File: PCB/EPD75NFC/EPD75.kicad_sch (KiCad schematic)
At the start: 149 parts, among them J1 Conn_01x26, J10 TF_PUSH, J11 Reset, J12 TC2030-USB-NL-DS, J2 PWR, J3 NFC, J4 BTN, J5 USB-C-Socket-H, J7 USB-C-Socket-H, J8 PWR, Q1 BSS138, SW2 Tamper, U2 PN532, U3 MD8942, U4 ESP32-S3-MINI-1, Y1 27.12MHz

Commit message: Tidy for new inductor
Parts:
- removed JP2: SolderJumper_3_Bridged12, RevK:SolderJumper3, symbol Jumper:SolderJumper_3_Bridged12
- removed R2: 3R, RevK:R_0402, symbol Device:R
- added C67: 220uF Tant, RevK:CP_EIA-3528-21_Kemet-B, symbol Device:C_Polarized
- added C68, C69: 22uF, RevK:C_0603, symbol Device:C
- added C70: 100nF, RevK:C_0402, symbol Device:C
- C17, C18: value 4.7uF -> 4.7uF 50V; footprint RevK:C_0402 -> RevK:C_0805
- L1: value 10uH -> 470uH; MPN (none) -> C42429207
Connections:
- net +3.3V: now also C67.1, C68.2, C69.2, C70.2
- net D-: now also J12.2 (NC), J12.6 (NC)
- net GND: now also C67.2, C68.1, C69.1, C70.1; no longer J12.6 (GND)
- net VBUS: no longer J12.2 (VBUS)
- net at R1.1: now also J1.3 (Pin_3), Q1.2 (S)
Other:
- moved on the sheet: R1

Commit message: Tamper
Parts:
- SW2: value Tamper -> ESE13V01D; footprint RevK:SW_Push_1P1T_NO_6x6mm -> RevK:ESE13; Manufacturer (none) -> Panasonic; Part No (none) -> ESE13V01D; now in the parts list
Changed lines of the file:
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@@
+	)
+	(symbol
+		(lib_id "Switch:SW_Push")
+		(at 481.965 142.875 0)
+		(unit 1)
+		(exclude_from_sim no)
+		(in_bom yes)
+		(on_board yes)
+		(dnp no)
+		(property "Reference" "SW2"
+			(at 481.965 135.636 0)
+			(effects
+				(font
+					(size 1.27 1.27)
+				)
+			)
+		)
+		(property "Value" "ESE13V01D"
+			(at 481.965 137.9474 0)
+			(effects
+				(font
+					(size 1.27 1.27)
+				)
+			)
+		)
+		(property "Footprint" "RevK:ESE13"
+			(at 481.965 137.795 0)
+			(effects
+				(font
+					(size 1.27 1.27)
+				)
+				(hide yes)
+			)
+		)
+		(property "Datasheet" "https://docs.rs-online.com/73f9/0900766b810acfc9.pdf"
+			(at 481.965 137.795 0)
+			(effects
+				(font
+					(size 1.27 1.27)
+				)
+				(hide yes)
+			)
+		)
+		(property "Description" ""
+			(at 481.965 142.875 0)
+			(effects
+				(font
+					(size 1.27 1.27)
+				)
+				(hide yes)
+			)
+		)
+		(property "Part No" "ESE13V01D"
+			(at 481.965 142.875 0)
+			(effects
+				(font
+					(size 1.27 1.27)
+				)
+				(hide yes)
+			)
+		)
+		(property "Manufacturer" "Panasonic"
+			(at 481.965 142.875 0)
+			(effects
+				(font
+					(size 1.27 1.27)
+				)
+				(hide yes)
+			)
+		)
+		(pin "1"
+		)
+		(pin "2"
+		)
+		(instances
+			(project "EPD75"
+				(path "/46c350bb-7de4-4e81-aafd-4af55e37aab0"
+					(reference "SW2")
+					(unit 1)
+				)
+			)
+		)
 	)
 	(symbol
@@
 					(unit 1)
 				)
-			)
-		)
-	)
-	(symbol
-		(lib_id "Switch:SW_Push")
-		(at 481.965 142.875 0)
-		(unit 1)
-		(exclude_from_sim no)
-		(in_bom no)
-		(on_board yes)
-		(dnp no)
-		(fields_autoplaced yes)
-		(property "Reference" "SW2"
-			(at 481.965 135.8095 0)
-			(effects
-				(font
-					(size 1.27 1.27)
-				)
-			)
-		)
-		(property "Value" "Tamper"
-			(at 481.965 138.2338 0)
-			(effects
-				(font
-					(size 1.27 1.27)
-				)
-			)
-		)
-		(property "Footprint" "RevK:SW_Push_1P1T_NO_6x6mm"
-			(at 481.965 137.795 0)
-			(effects
-				(font
-					(size 1.27 1.27)
-				)
-				(hide yes)
-			)
-		)
-		(property "Datasheet" "~"
-			(at 481.965 137.795 0)
-			(effects
-				(font
-					(size 1.27 1.27)
-				)
-				(hide yes)
-			)
-		)
-		(property "Description" "Push button switch, generic, two pins"
-			(at 481.965 142.875 0)
-			(effects
-				(font
-					(size 1.27 1.27)
-				)
-				(hide yes)
-			)
-		)
-		(pin "1"
-		)
-		(pin "2"
-		)
-		(instances
-			(project "EPD75"
-				(path "/46c350bb-7de4-4e81-aafd-4af55e37aab0"
-					(reference "SW2")
-					(unit 1)
-				)

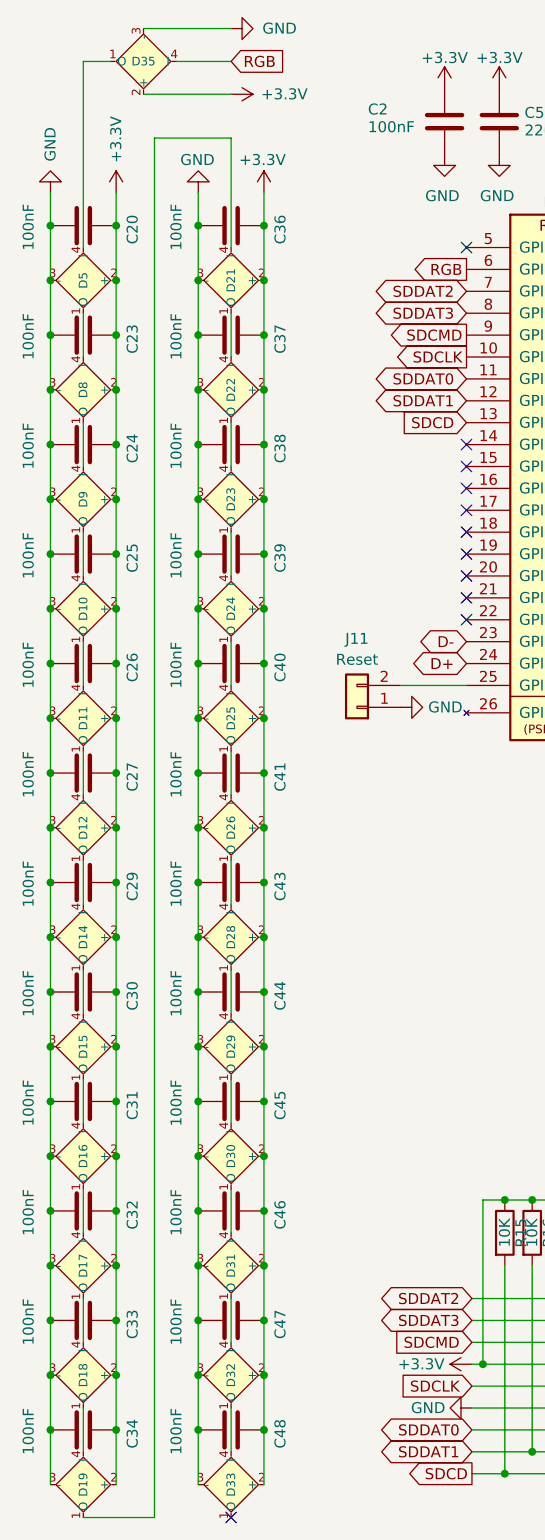
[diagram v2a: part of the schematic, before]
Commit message: New LEDs
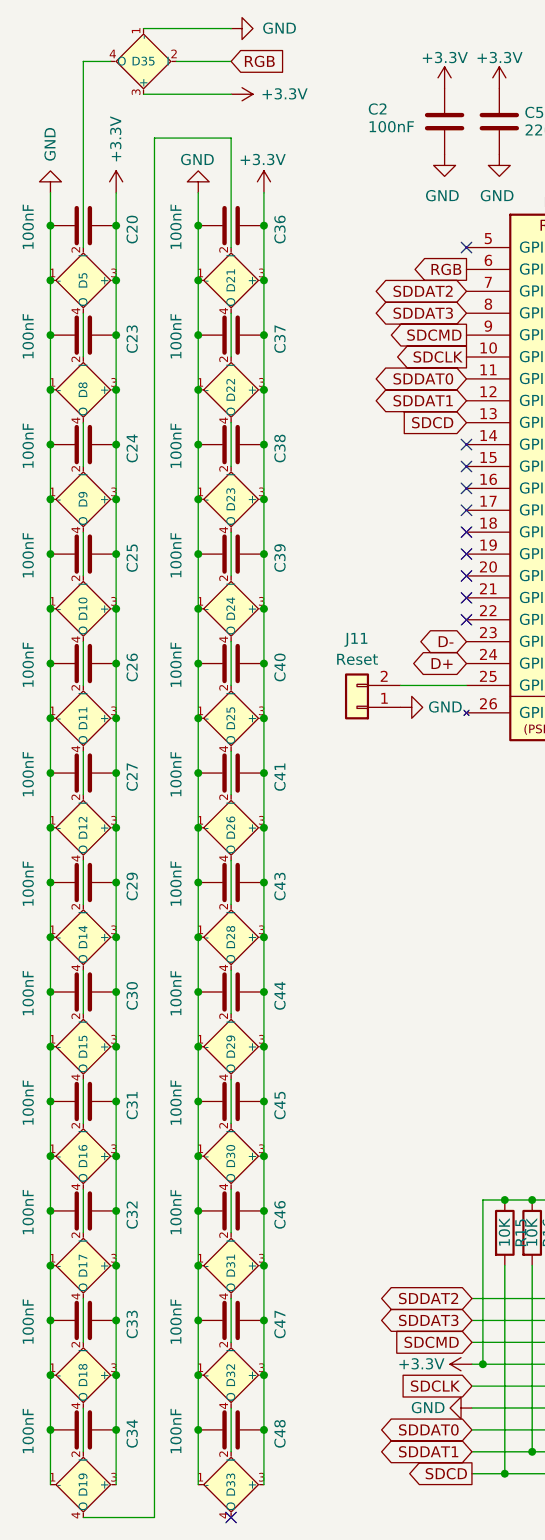
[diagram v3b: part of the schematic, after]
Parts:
- D10, D11, D12, D14, D15, D16, D17, D18, D19, D21, D22, D23, D24, D25, D26, D28, D29, D30, D31, D32, D33, D35, D5, D8, D9: footprint RevK:SMD1010 -> RevK:SMD1615; symbol RevK:WS2812B-1mm -> RevK:WS2812B-1.5mm; MPN C5349953 -> C5349954
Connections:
- net +3.3V: now also D10.3 (+), D11.3 (+), D12.3 (+), D14.3 (+), D15.3 (+), D16.3 (+), D17.3 (+), D18.3 (+), D19.3 (+), D21.3 (+), D22.3 (+), D23.3 (+), D24.3 (+), D25.3 (+), D26.3 (+), D28.3 (+), D29.3 (+), D30.3 (+), D31.3 (+), D32.3 (+), D33.3 (+), D35.3 (+), D5.3 (+), D8.3 (+), D9.3 (+); no longer D10.2 (+), D11.2 (+), D12.2 (+), D14.2 (+), D15.2 (+), D16.2 (+), D17.2 (+), D18.2 (+), D19.2 (+), D21.2 (+), D22.2 (+), D23.2 (+), D24.2 (+), D25.2 (+), D26.2 (+), D28.2 (+), D29.2 (+), D30.2 (+), D31.2 (+), D32.2 (+), D33.2 (+), D35.2 (+), D5.2 (+), D8.2 (+), D9.2 (+)
- net GND: now also D10.1 (-), D11.1 (-), D12.1 (-), D14.1 (-), D15.1 (-), D16.1 (-), D17.1 (-), D18.1 (-), D19.1 (-), D21.1 (-), D22.1 (-), D23.1 (-), D24.1 (-), D25.1 (-), D26.1 (-), D28.1 (-), D29.1 (-), D30.1 (-), D31.1 (-), D32.1 (-), D33.1 (-), D35.1 (-), D5.1 (-), D8.1 (-), D9.1 (-); no longer D10.3 (-), D11.3 (-), D12.3 (-), D14.3 (-), D15.3 (-), D16.3 (-), D17.3 (-), D18.3 (-), D19.3 (-), D21.3 (-), D22.3 (-), D23.3 (-), D24.3 (-), D25.3 (-), D26.3 (-), D28.3 (-), D29.3 (-), D30.3 (-), D31.3 (-), D32.3 (-), D33.3 (-), D35.3 (-), D5.3 (-), D8.3 (-), D9.3 (-)
- net RGB: now also D35.2 (I); no longer D35.4 (I)
- net at D22.4 (O): now also D23.2 (I); no longer D21.1 (O)
- net at D21.4 (O): now also D22.2 (I); no longer D19.1 (O)
- net at D19.4 (O): now also D21.2 (I); no longer D18.1 (O)
- net at D23.4 (O): now also D24.2 (I); no longer D22.1 (O)
- net at D30.4 (O): now also D31.2 (I); no longer D29.1 (O)
- net at D29.4 (O): now also D30.2 (I); no longer D28.1 (O)
- net at D24.4 (O): now also D25.2 (I); no longer D23.1 (O)
- net at D28.4 (O): now also D29.2 (I); no longer D26.1 (O)
- net at D26.4 (O): now also D28.2 (I); no longer D25.1 (O)
- net at D17.4 (O): now also D18.2 (I); no longer D16.1 (O)
- net at D16.4 (O): now also D17.2 (I); no longer D15.1 (O)
- net at D18.4 (O): now also D19.2 (I); no longer D17.1 (O)
- net at D14.4 (O): now also D15.2 (I); no longer D12.1 (O)
- net at D12.4 (O): now also D14.2 (I); no longer D11.1 (O)
- net at D31.4 (O): now also D32.2 (I); no longer D30.1 (O)
- net at D33.4 (O): no longer D32.1 (O)
- net at D32.4 (O): now also D33.2 (I); no longer D31.1 (O)
- net at D9.4 (O): now also D10.2 (I); no longer D8.1 (O)
- net at D8.4 (O): now also D9.2 (I); no longer D5.1 (O)
- net at D25.4 (O): now also D26.2 (I); no longer D24.1 (O)
- net at D11.4 (O): now also D12.2 (I); no longer D10.1 (O)
- net at D5.4 (O): now also D8.2 (I); no longer D35.1 (O)
- net at D15.4 (O): now also D16.2 (I); no longer D14.1 (O)
- net at D10.4 (O): now also D11.2 (I); no longer D9.1 (O)
- new net: D35.4 (O), D5.2 (I)
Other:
- moved on the sheet: D10, D11, D12, D14, D15, D16, D17, D18, D19, D21, D22, D23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

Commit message: Regulator update
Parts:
- removed C10: 100nF, RevK:C_0603_, symbol RevK:Hidden
- removed C8: 10uF 35V, RevK:C_0603_, symbol RevK:Hidden
- removed C9: 10uF 6.3V, RevK:C_0603_, symbol RevK:Hidden
- removed L2: 10uH, RevK:L_4x4_, symbol RevK:Hidden
- removed R10: 39k2, RevK:R_0402_, symbol RevK:Hidden
- removed R11: 1M, RevK:R_0402_, symbol RevK:Hidden
- removed R9: 124k, RevK:R_0402_, symbol RevK:Hidden
- removed U3: MD8942, RevK:SOT-23-6-MD8942, symbol RevK:MD89420-RegBlock
- added C21: 22uF 25V, RevK:C_0805, symbol Device:C
- added C71, C72: 100nF 25V, RevK:C_0402, symbol Device:C
- added C73, C76, C77, C78, C79, C80: 100nF, RevK:C_0201, symbol Device:C
- added C74: 18pF, RevK:C_0201, symbol Device:C
- added C75: 47uF 6V, RevK:C_0805, symbol Device:C
- added L5: 4.7uH, RevK:L_5x5, symbol Device:L
- added R14, R2: 150k 1%, RevK:R_0201, symbol Device:R
- added R29: 33k 1%, RevK:R_0201, symbol Device:R
- added U1: TPS562246, RevK:SOT-563, symbol RevK:TPS562246
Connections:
- net +3.3V: now also C74.2, C75.1, C76.2, C77.2, C78.2, C79.2, C80.2, L5.2, R14.1
- net GND: now also C21.2, C71.2, C72.2, C75.2, C76.1, C77.1, C78.1, C79.1, C80.1, R29.2, U1.3 (GND)
- net PWR: now also C21.1, C71.1, C72.1, R2.2, U1.1 (VIN)
- new net BST: C73.1, U1.4 (VBST)
- new net EN: R2.1, U1.5 (EN)
- new net FB: C74.1, R14.2, R29.1, U1.6 (VFB)
- new net SW: C73.2, L5.1, U1.2 (SW)
- no-connect marks 41 -> 40
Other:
- moved on the sheet: C19, C22, D34, J4, J8, R7

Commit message: Library update
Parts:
- L1: footprint RevK:L_4x4 -> RevK:L_6x6; MPN C42429207 -> C168100
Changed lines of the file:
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@@
 			)
 		)
-		(property "Footprint" "RevK:L_4x4"
+		(property "Footprint" "RevK:L_6x6"
 			(at 187.96 93.98 0)
 			(effects
@@
 			)
 		)
-		(property "MPN" "C42429207"
+		(property "MPN" "C168100"
 			(at 187.96 93.98 0)
 			(effects

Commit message: Library update
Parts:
- added C8, C81, C83, C9: 100nF, RevK:C_0201, symbol Device:C
- added T1: T3902_MEMS_Mic, RevK:T3902_MEMS_Mic_Open, symbol RevK:T3902_MEMS_Mic
- added U3: SCD41, RevK:SCD41, symbol RevK:SCD41
- added U5: GZP6816D, RevK:Bosch_LGA-8_2x2.5mm_P0.65mm_ClockwisePinNumbering, symbol RevK:GZP6816D
- added U7: SHT40, RevK:Sensirion_DFN-4_1.5x1.5mm_P0.5mm_SHT4x-Side, symbol RevK:SHT40
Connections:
- net +3.3V: now also C8.2, C81.2, C83.2, C9.2, T1.2 (SELECT), T1.5 (VDD), U3.19 (VDDH), U3.7 (VDD), U5.8 (VDD), U7.3 (VDD)
- net GND: now also C8.1, C81.1, C83.1, C9.1, T1.3 (GND), U3.20 (GND), U3.21 (GND), U3.6 (GND), U5.1 (GND), U5.7 (GND), U7.4 (VSS)
- net SCL: now reaches U4.19 (GPIO15)
- net SCL: now also U3.9 (SCL), U5.4 (SCL), U7.2 (SCL)
- net SDA: now reaches U4.20 (GPIO16)
- net SDA: now also U3.10 (SDA), U5.3 (SDA), U7.1 (SDA)
- net MDATA: now reaches U4.21 (GPIO17)
- net MDATA: now also T1.1 (DATA)
- net MCLK: now reaches U4.22 (GPIO18)
- net MCLK: now also T1.4 (CLK)
- no-connect marks 40 -> 36
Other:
- note added: "Left"
- moved on the sheet: A1, C35, C42, C49, C50, C51, C52, C53, C54, C55, C56, C57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

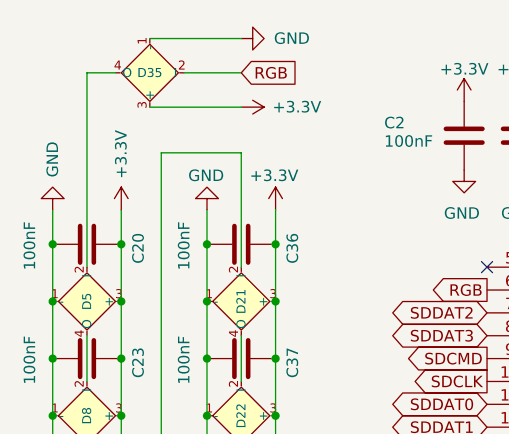
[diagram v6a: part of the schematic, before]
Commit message: Updated NFC, and re-render
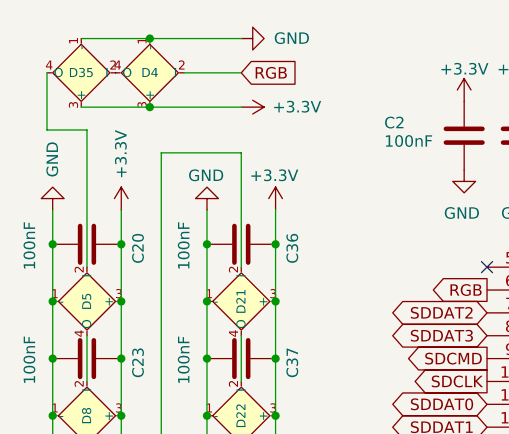
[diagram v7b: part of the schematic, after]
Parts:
- added D4: XL-1010RGBC-WS2812B, RevK:SMD1615, symbol RevK:WS2812B-1.5mm
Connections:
- net +3.3V: now also D4.3 (+)
- net GND: now also D4.1 (-)
- net RGB: now also D4.2 (I); no longer D35.2 (I)
- new net: D35.2 (I), D4.4 (O)
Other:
- moved on the sheet: D35
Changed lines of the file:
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@@
 	)
 	(junction
+		(at 31.115 16.51)
+		(diameter 0)
+		(color 0 0 0 0)
+	)
+	(junction
 		(at 27.94 77.47)
 		(diameter 0)
@@
 	)
 	(junction
+		(at 31.115 24.13)
+		(diameter 0)
+		(color 0 0 0 0)
+	)
+	(junction
 		(at 269.24 37.465)
 		(diameter 0)
@@
 	(wire
 		(pts
+			(xy 23.495 16.51) (xy 31.115 16.51)
+		)
+		(stroke
+			(width 0)
+			(type default)
+		)
+	)
+	(wire
+		(pts
 			(xy 204.47 271.145) (xy 204.47 303.53)
 		)
@@
 	(wire
 		(pts
+			(xy 31.115 16.51) (xy 41.275 16.51)
+		)
+		(stroke
+			(width 0)
+			(type default)
+		)
+	)
+	(wire
+		(pts
 			(xy 41.275 181.61) (xy 41.275 176.53)
 		)
@@
 	(wire
 		(pts
+			(xy 19.685 20.32) (xy 19.685 26.67)
+		)
+		(stroke
+			(width 0)
+			(type default)
+		)
+	)
+	(wire
+		(pts
 			(xy 20.32 71.12) (xy 20.32 77.47)
 		)
@@
 	(wire
 		(pts
-			(xy 27.305 20.32) (xy 24.13 20.32)
-		)
-		(stroke
-			(width 0)
-			(type default)
-		)
-	)
-	(wire
-		(pts
 			(xy 20.32 39.37) (xy 20.32 45.72)
 		)
@@
 	(wire
 		(pts
+			(xy 23.495 24.13) (xy 31.115 24.13)
+		)
+		(stroke
+			(width 0)
+			(type default)
+		)
+	)
+	(wire
+		(pts
 			(xy 37.465 58.42) (xy 37.465 64.77)
 		)
@@
 	(wire
 		(pts
-			(xy 31.115 16.51) (xy 41.275 16.51)
+			(xy 184.785 27.305) (xy 186.055 27.305)
 		)
 		(stroke
@@
 	(wire
 		(pts
-			(xy 184.785 27.305) (xy 186.055 27.305)
+			(xy 27.94 35.56) (xy 27.94 39.37)
 		)
 		(stroke
@@
 	(wire
 		(pts
-			(xy 27.94 35.56) (xy 27.94 39.37)
+			(xy 70.485 171.45) (xy 96.52 171.45)
 		)
 		(stroke
@@
 	(wire
 		(pts
-			(xy 70.485 171.45) (xy 96.52 171.45)
+			(xy 37.465 147.32) (xy 37.465 153.67)
 		)
 		(stroke
@@
 	(wire
 		(pts
-			(xy 37.465 147.32) (xy 37.465 153.67)
+			(xy 37.465 83.82) (xy 37.465 90.17)
 		)
 		(stroke
@@
 	(wire
 		(pts
-			(xy 37.465 83.82) (xy 37.465 90.17)
+			(xy 24.13 26.67) (xy 24.13 41.91)
 		)
 		(stroke
@@
 	(wire
 		(pts
-			(xy 24.13 20.32) (xy 24.13 41.91)
-		)
-		(stroke
-			(width 0)
-			(type default)
-		)
-	)
-	(wire
-		(pts
 			(xy 144.145 207.01) (xy 153.035 207.01)
 		)
@@
 	(wire
 		(pts
+			(xy 31.115 24.13) (xy 41.275 24.13)
+		)
+		(stroke
+			(width 0)
+			(type default)
+		)
+	)
+	(wire
+		(pts
 			(xy 235.585 282.575) (xy 231.775 282.575)
 		)
@@
 	(wire
 		(pts
+			(xy 19.685 26.67) (xy 24.13 26.67)
+		)
+		(stroke
+			(width 0)
+			(type default)
+		)
+	)
+	(wire
+		(pts
 			(xy 99.06 95.885) (xy 105.41 95.885)
 		)
@@
 	(wire
 		(pts
-			(xy 31.115 24.13) (xy 41.275 24.13)
-		)
-		(stroke
-			(width 0)
-			(type default)
-		)
-	)
-	(wire
-		(pts
 			(xy 114.935 268.605) (xy 139.065 268.605)
 		)
@@
 	)
 	(symbol
+		(lib_id "RevK:WS2812B-1.5mm")
+		(at 31.115 20.32 180)
+		(unit 1)
+		(exclude_from_sim no)
+		(in_bom yes)
+		(on_board yes)
+		(dnp no)
+		(property "Reference" "D4"
+			(at 31.115 20.32 0)
+			(do_not_autoplace yes)
+			(effects
+				(font
+					(size 1 1)
+				)
+			)
+		)
+		(property "Value" "XL-1010RGBC-WS2812B"
+			(at 29.845 14.605 0)
+			(effects
+				(font
+					(size 1 1)
+				)
+				(justify left top)
+				(hide yes)
+			)
+		)
+		(property "Footprint" "RevK:SMD1615"
+			(at 29.845 27.94 0)
+			(effects
+				(font
+					(size 1 1)
+				)
+				(justify left top)
+				(hide yes)
+			)
+		)
+		(property "Datasheet" "https://datasheet.lcsc.com/lcsc/2301111010_XINGLIGHT-XL-1010RGBC-WS2812B_C5349953.pdf"
+			(at 29.845 29.845 0)
+			(effects
+				(font
+					(size 1 1)
+				)
+				(justify left top)
+				(hide yes)
+			)
+		)
+		(property "Description" "RGB LED with integrated controller"
+			(at 31.115 20.32 0)
+			(effects
+				(font
+					(size 1.27 1.27)
+				)
+				(hide yes)
+			)
+		)
+		(property "MPN" "C5349954"
+			(at 29.845 31.75 0)
+			(effects
+				(font
+					(size 1 1)
+				)
+				(justify left top)
+				(hide yes)
+			)
+		)
+		(pin "1"
+		)
+		(pin "2"
+		)
+		(pin "3"
+		)
+		(pin "4"
+		)
+		(instances
+			(project "EPD75"
+				(path "/46c350bb-7de4-4e81-aafd-4af55e37aab0"
+					(reference "D4")
+					(unit 1)
+				)
+			)
+		)
+	)
+	(symbol
 		(lib_id "power:GND")
 		(at 209.55 149.225 0)
@@
 	(symbol
 		(lib_id "RevK:WS2812B-1.5mm")
-		(at 31.115 20.32 180)
+		(at 23.495 20.32 180)
 		(unit 1)
 		(exclude_from_sim no)
@@
 		(dnp no)
 		(property "Reference" "D35"
-			(at 31.115 20.32 0)
+			(at 23.495 20.32 0)
 			(do_not_autoplace yes)
 			(effects
@@
 		)
 		(property "Value" "XL-1010RGBC-WS2812B"
-			(at 29.845 14.605 0)
+			(at 22.225 14.605 0)
 			(effects
 				(font
@@
 		)
 		(property "Footprint" "RevK:SMD1615"
-			(at 29.845 27.94 0)
+			(at 22.225 27.94 0)
 			(effects
 				(font
@@
 		)
 		(property "Datasheet" "https://datasheet.lcsc.com/lcsc/2301111010_XINGLIGHT-XL-1010RGBC-WS2812B_C5349953.pdf"
-			(at 29.845 29.845 0)
+			(at 22.225 29.845 0)
 			(effects
 				(font
@@
 		)
 		(property "Description" "RGB LED with integrated controller"
-			(at 31.115 20.32 0)
+			(at 23.495 20.32 0)
 			(effects
 				(font
@@
 		)
 		(property "MPN" "C5349954"
-			(at 29.845 31.75 0)
+			(at 22.225 31.75 0)
 			(effects
 				(font
